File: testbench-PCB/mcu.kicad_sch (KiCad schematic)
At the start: 16 parts, among them J2 AVR-ISP-6, SW1 RESET, U1 ATmega2561-16A, Y1 X322516MLB4SI

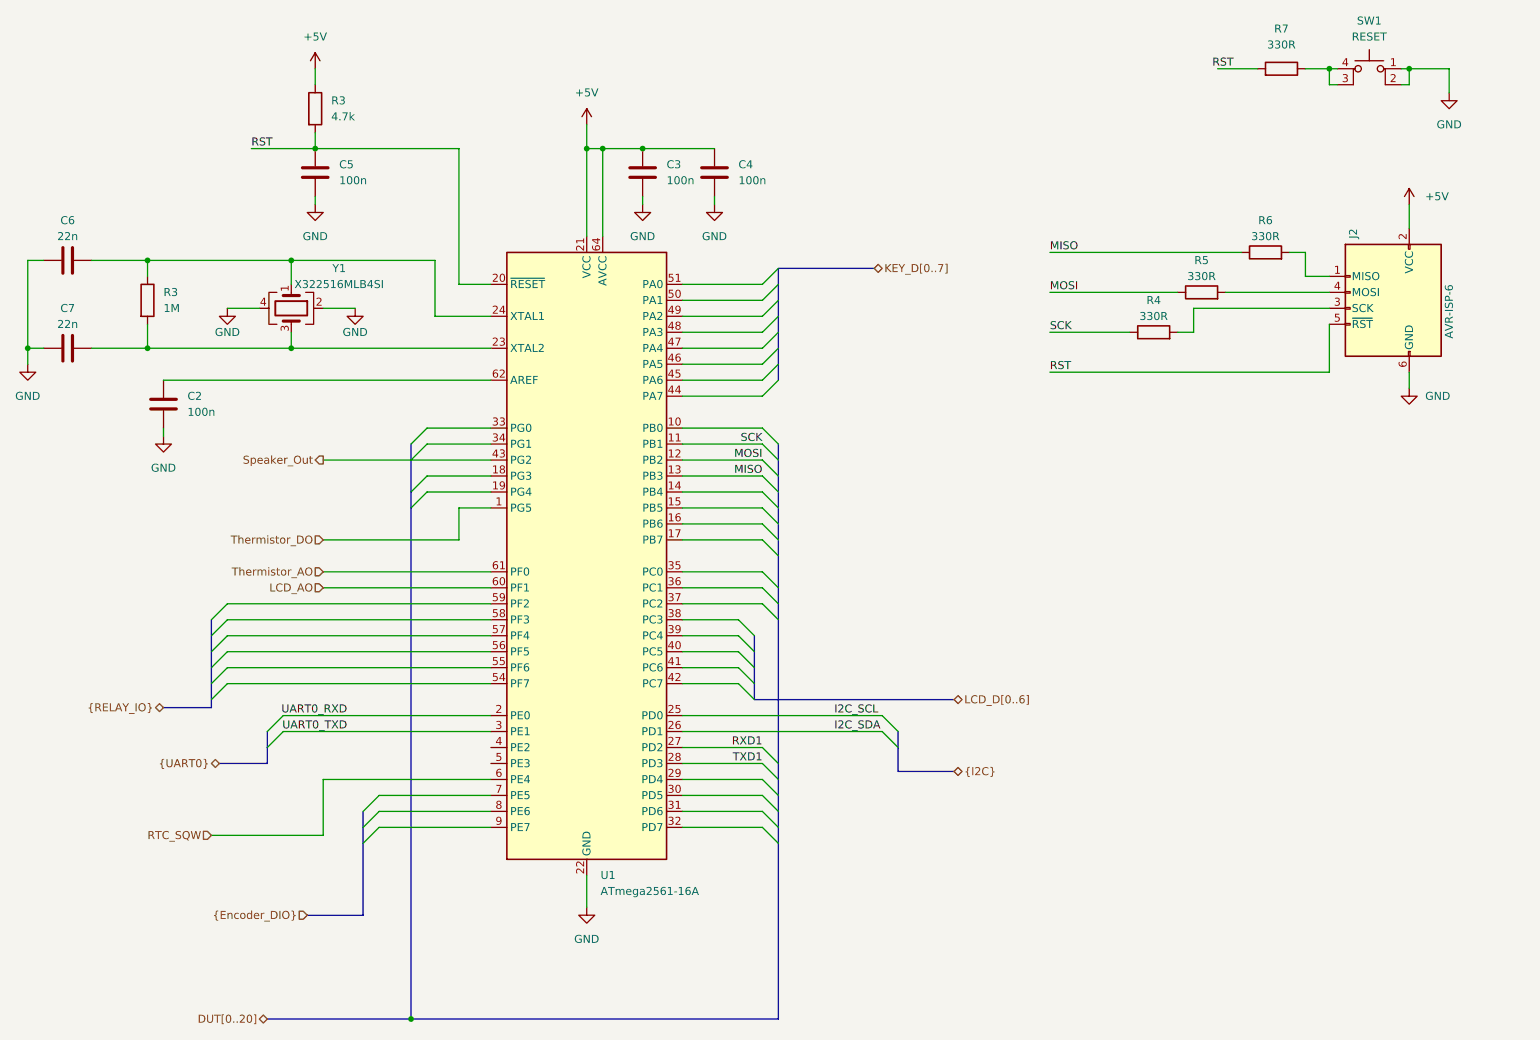
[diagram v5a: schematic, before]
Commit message: Connecter speaker, added JTAG.
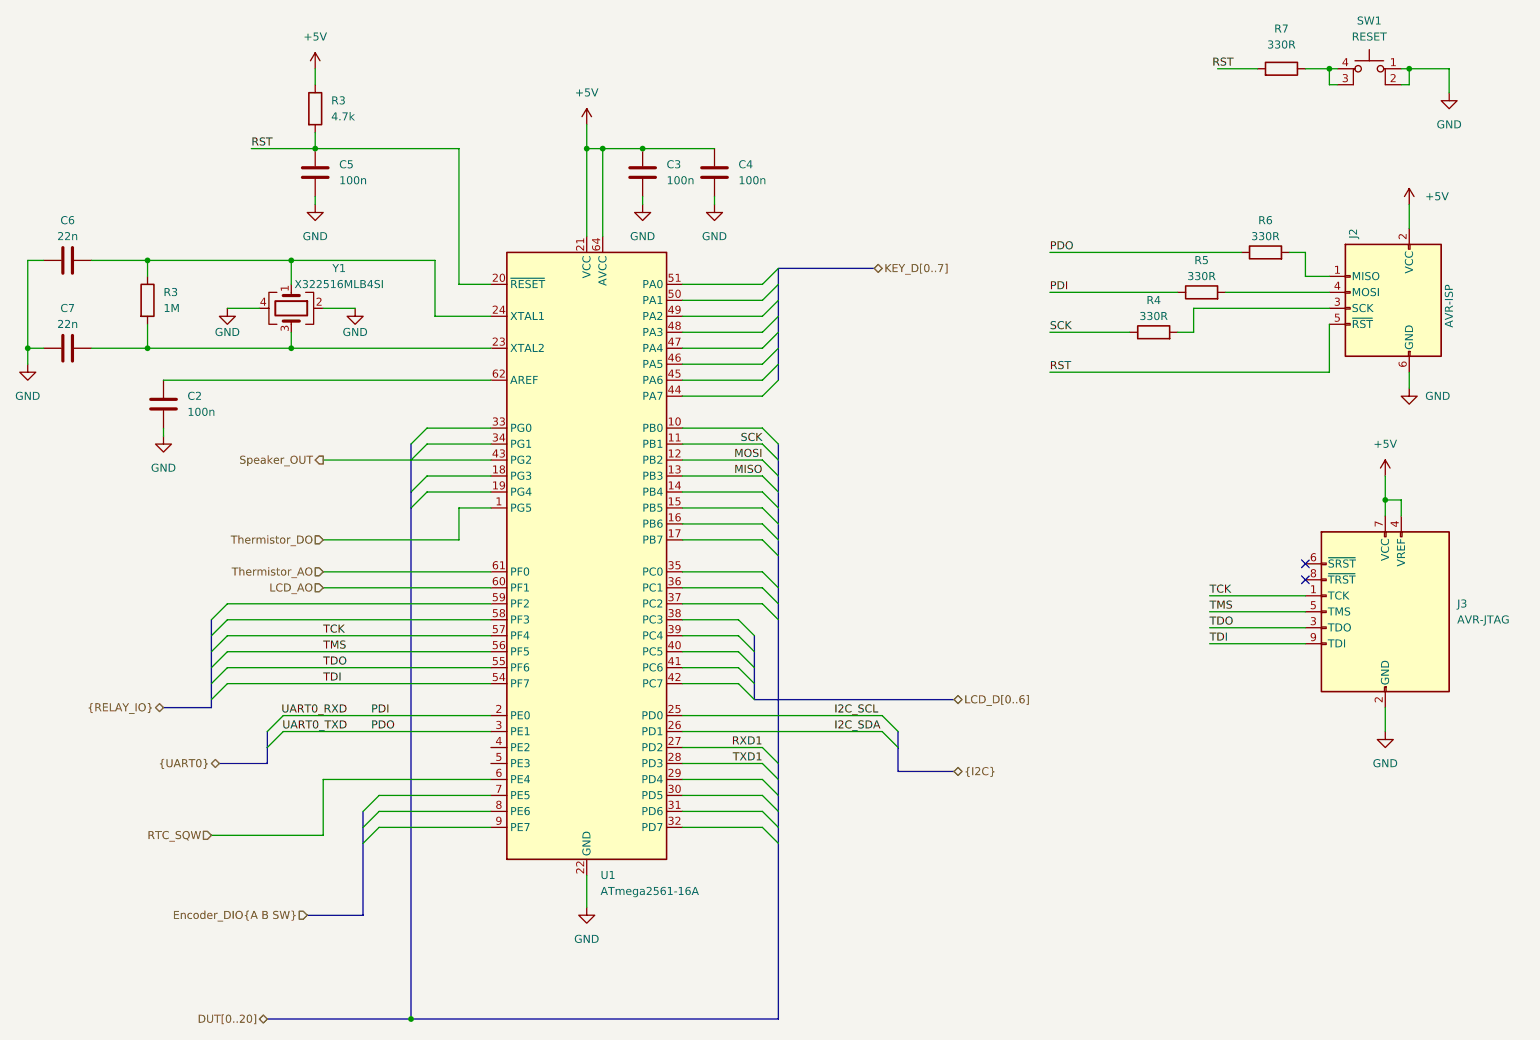
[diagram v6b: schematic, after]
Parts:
- added J3: AVR-JTAG, Connector_IDC:IDC-Header_2x05_P2.54mm_Vertical, symbol Connector:AVR-JTAG-10
- J2: value AVR-ISP-6 -> AVR-ISP
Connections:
- net +5V: now also J3.4 (VREF), J3.7 (VCC)
- net GND: now also J3.10 (GND), J3.2 (GND)
- net MISO: no longer R6.1
- net MOSI: no longer R5.1
- net TDI: now reaches U1.54 (PF7)
- net TDI: now also J3.9 (TDI)
- net TDO: now reaches U1.55 (PF6)
- net TDO: now also J3.3 (TDO)
- net TMS: now reaches U1.56 (PF5)
- net TMS: now also J3.5 (TMS)
- net TCK: now reaches U1.57 (PF4)
- net TCK: now also J3.1 (TCK)
- net Speaker_Out renamed Speaker_OUT
- net UART0_RXD renamed PDI
- net PDI: now also R5.1
- net UART0_TXD renamed PDO
- net PDO: now also R6.1
- no-connect marks 0 -> 2

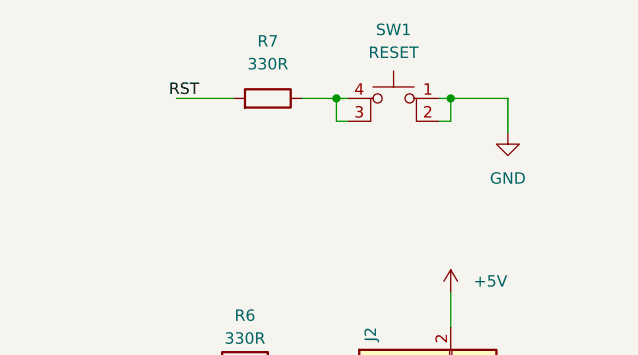
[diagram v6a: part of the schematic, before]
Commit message: Created PCB, changed footprints for symbols.
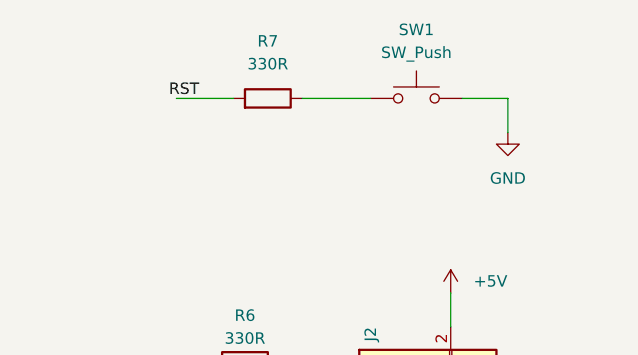
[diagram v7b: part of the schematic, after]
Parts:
- removed SW1: RESET, symbol Switch:SW_MEC_5E
- added SW1: SW_Push, Button_Switch_SMD:SW_Push_1P1T_XKB_TS-1187A, symbol Switch:SW_Push
- Y1: footprint (none) -> Oscillator:Oscillator_SMD_Abracon_ASE-4Pin_3.2x2.5mm
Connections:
- net GND: now also SW1.2
- net at R7.1: now also SW1.1
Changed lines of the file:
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@@
   (paper "A4")
   (bus_alias "UART1" (members "UART1_TXD" "UART1_RXD"))
-  (junction (at 246.38 33.02) (diameter 0) (color 0 0 0 0)
-  )
   (junction (at 81.28 63.5) (diameter 0) (color 0 0 0 0)
   )
@@
   )
   (junction (at 39.37 77.47) (diameter 0) (color 0 0 0 0)
-  )
-  (junction (at 259.08 33.02) (diameter 0) (color 0 0 0 0)
   )
   (junction (at 137.16 45.72) (diameter 0) (color 0 0 0 0)
@@
     (stroke (width 0) (type default))
   )
-  (wire (pts (xy 259.08 35.56) (xy 257.81 35.56))
-    (stroke (width 0) (type default))
-  )
   (wire (pts (xy 71.12 71.12) (xy 76.2 71.12))
     (stroke (width 0) (type default))
@@
     (stroke (width 0) (type default))
   )
-  (wire (pts (xy 246.38 33.02) (xy 242.57 33.02))
-    (stroke (width 0) (type default))
-  )
   (bus (pts (xy 154.94 125.73) (xy 154.94 128.27))
     (stroke (width 0) (type default))
@@
     (stroke (width 0) (type default))
   )
-  (wire (pts (xy 257.81 33.02) (xy 259.08 33.02))
-    (stroke (width 0) (type default))
-  )
   (wire (pts (xy 137.16 53.34) (xy 137.16 54.61))
     (stroke (width 0) (type default))
@@
     (stroke (width 0) (type default))
   )
-  (wire (pts (xy 247.65 33.02) (xy 246.38 33.02))
-    (stroke (width 0) (type default))
-  )
   (wire (pts (xy 130.81 59.69) (xy 130.81 45.72))
     (stroke (width 0) (type default))
@@
     (stroke (width 0) (type default))
   )
+  (wire (pts (xy 260.35 33.02) (xy 265.43 33.02))
+    (stroke (width 0) (type default))
+  )
   (wire (pts (xy 143.51 82.55) (xy 156.21 82.55))
     (stroke (width 0) (type default))
@@
     (stroke (width 0) (type default))
   )
-  (wire (pts (xy 259.08 33.02) (xy 259.08 35.56))
-    (stroke (width 0) (type default))
-  )
   (wire (pts (xy 113.03 95.25) (xy 100.33 95.25))
     (stroke (width 0) (type default))
   )
-  (wire (pts (xy 265.43 33.02) (xy 259.08 33.02))
-    (stroke (width 0) (type default))
-  )
   (bus (pts (xy 69.85 143.51) (xy 77.47 143.51))
     (stroke (width 0) (type default))
@@
     (stroke (width 0) (type default))
   )
-  (wire (pts (xy 247.65 35.56) (xy 246.38 35.56))
-    (stroke (width 0) (type default))
-  )
   (wire (pts (xy 107.95 102.87) (xy 113.03 102.87))
     (stroke (width 0) (type default))
@@
     (stroke (width 0) (type default))
   )
+  (wire (pts (xy 242.57 33.02) (xy 250.19 33.02))
+    (stroke (width 0) (type default))
+  )
   (wire (pts (xy 102.87 92.71) (xy 113.03 92.71))
     (stroke (width 0) (type default))
@@
   )
   (wire (pts (xy 255.27 134.62) (xy 255.27 138.43))
-    (stroke (width 0) (type default))
-  )
-  (wire (pts (xy 246.38 33.02) (xy 246.38 35.56))
     (stroke (width 0) (type default))
   )
@@
       (effects (font (size 1.27 1.27)))
     )
-    (property "Footprint" "" (at 81.28 71.12 0)
+    (property "Footprint" "Oscillator:Oscillator_SMD_Abracon_ASE-4Pin_3.2x2.5mm" (at 81.28 71.12 0)
       (effects (font (size 1.27 1.27)) hide)
     )
@@
         (path "/3ac6901d-218d-4b34-8c4a-bf7c417c33bc/08a6730c-9a7c-47f6-b930-4f7799d77218"
           (reference "#PWR012") (unit 1)
-        )
-      )
-    )
-  )
-  (symbol (lib_id "Switch:SW_MEC_5E") (at 252.73 35.56 0) (mirror y) (unit 1)
-    (in_bom yes) (on_board yes) (dnp no) (fields_autoplaced)
-    (property "Reference" "SW1" (at 252.73 25.4 0)
-      (effects (font (size 1.27 1.27)))
-    )
-    (property "Value" "RESET" (at 252.73 27.94 0)
-      (effects (font (size 1.27 1.27)))
-    )
-    (property "Footprint" "" (at 252.73 27.94 0)
-      (effects (font (size 1.27 1.27)) hide)
-    )
-    (property "Datasheet" "http://www.apem.com/int/index.php?controller=attachment&id_attachment=1371" (at 252.73 27.94 0)
-      (effects (font (size 1.27 1.27)) hide)
-    )
-    (pin "1")
-    (pin "2")
-    (pin "3")
-    (pin "4")
-    (instances
-      (project "testbench"
-        (path "/3ac6901d-218d-4b34-8c4a-bf7c417c33bc"
-          (reference "SW1") (unit 1)
-        )
-        (path "/3ac6901d-218d-4b34-8c4a-bf7c417c33bc/08a6730c-9a7c-47f6-b930-4f7799d77218"
-          (reference "SW1") (unit 1)
         )
       )
@@
         )
       )
+    )
+  )
+  (symbol (lib_id "Switch:SW_Push") (at 255.27 33.02 0) (unit 1)
+    (in_bom yes) (on_board yes) (dnp no) (fields_autoplaced)
+    (property "Reference" "SW1" (at 255.27 25.4 0)
+      (effects (font (size 1.27 1.27)))
+    )
+    (property "Value" "SW_Push" (at 255.27 27.94 0)
+      (effects (font (size 1.27 1.27)))
+    )
+    (property "Footprint" "Button_Switch_SMD:SW_Push_1P1T_XKB_TS-1187A" (at 255.27 27.94 0)
+      (effects (font (size 1.27 1.27)) hide)
+    )
+    (property "Datasheet" "~" (at 255.27 27.94 0)
+      (effects (font (size 1.27 1.27)) hide)
+    )
+    (pin "1")
+    (pin "2")
+    (instances
+      (project "testbench"
+        (path "/3ac6901d-218d-4b34-8c4a-bf7c417c33bc/08a6730c-9a7c-47f6-b930-4f7799d77218"
+          (reference "SW1") (unit 1)
+        )
+      )

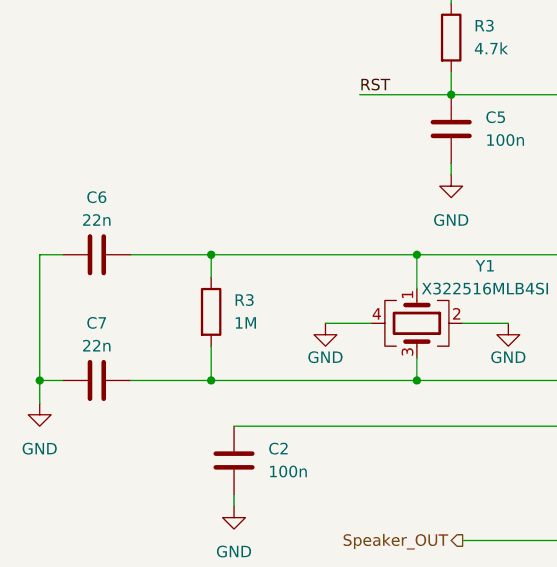
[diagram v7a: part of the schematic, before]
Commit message: Routed osc., USB interface.
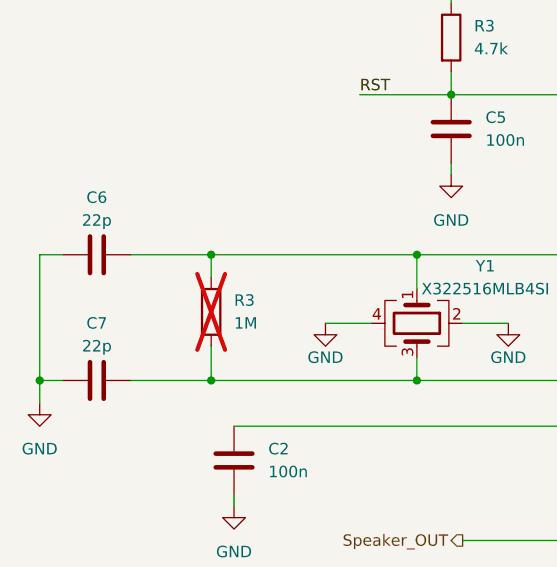
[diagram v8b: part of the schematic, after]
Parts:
- C6, C7: value 22n -> 22p
- R3: now not fitted
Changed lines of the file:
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@@
       (effects (font (size 1.27 1.27)))
     )
-    (property "Value" "22n" (at 45.72 73.66 90)
+    (property "Value" "22p" (at 45.72 73.66 90)
       (effects (font (size 1.27 1.27)))
     )
@@
   )
   (symbol (lib_id "Device:R") (at 58.42 69.85 0) (unit 1)
-    (in_bom yes) (on_board yes) (dnp no) (fields_autoplaced)
+    (in_bom yes) (on_board yes) (dnp yes) (fields_autoplaced)
     (property "Reference" "R3" (at 60.96 68.58 0)
       (effects (font (size 1.27 1.27)) (justify left))
@@
       (effects (font (size 1.27 1.27)))
     )
-    (property "Value" "22n" (at 45.72 59.69 90)
-      (effects (font (size 1.27 1.27)))
-    )
+    (property "Value" "22p" (at 45.72 59.69 90)
+      (effects (font (size 1.27 1.27)))
+    )
